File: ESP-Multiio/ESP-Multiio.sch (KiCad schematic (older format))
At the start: 40 parts, among them J1 Conn_01x10, SW1 SW_SPDT_MSM, SW2 SW_SPDT_MSM, SW3 SW_SPDT_MSM, SW4 SW_SPDT_MSM, U1 WeMos_D1_mini, U2 MCP23017_SP

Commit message: +IR
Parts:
- added C2: 100 nF, Capacitor_SMD:C_1206_3216Metric_Pad1.42x1.75mm_HandSolder, symbol Device:C
- added D-IR1: LED, LED_THT:LED_D3.0mm, symbol Device:LED
- added Q1: BC337, Package_TO_SOT_THT:TO-92_Inline, symbol Transistor_BJT:BC337
- added R10: 53 Ω, Resistor_SMD:R_1206_3216Metric_Pad1.42x1.75mm_HandSolder, symbol Device:R
- added R11: 33 kΩ, Resistor_SMD:R_1206_3216Metric_Pad1.42x1.75mm_HandSolder, symbol Device:R
- added R12: 100Ω, Resistor_SMD:R_1206_3216Metric_Pad1.42x1.75mm_HandSolder, symbol Device:R
- added R9: 2.1kΩ, Resistor_SMD:R_1206_3216Metric_Pad1.42x1.75mm_HandSolder, symbol Device:R
- added U4: TSOP1838, TSOP1838:TSOP18XX, symbol TSOP1838:TSOP1838
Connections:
- net +3V3: now also D-IR1.2 (A), R12.1
- net D0: now also R11.2, U4.OUT
- net D7: now also R9.2
- net GND: now also C2.2, Q1.3 (E), U4.GND
- net GPB0: now reaches SW1.3, U2.1 (GPB0)
- net GPB1: now reaches SW1.1, U2.2 (GPB1)
- net GPA0: now reaches R1.2, U2.21 (GPA0)
- net GPA1: now reaches R2.2, U2.22 (GPA1)
- net GPA2: now reaches R3.2, U2.23 (GPA2)
- net GPA3: now reaches R4.2, U2.24 (GPA3)
- net GPA4: now reaches R5.2, U2.25 (GPA4)
- net GPA5: now reaches R6.2, U2.26 (GPA5)
- net GPA6: now reaches R7.2, U2.27 (GPA6)
- net GPA7: now reaches R8.2, U2.28 (GPA7)
- net GPB2: now reaches SW2.3, U2.3 (GPB2)
- net GPB3: now reaches SW2.1, U2.4 (GPB3)
- net GPB4: now reaches SW3.3, U2.5 (GPB4)
- net GPB5: now reaches SW3.1, U2.6 (GPB5)
- net GPB6: now reaches SW4.3, U2.7 (GPB6)
- net GPB7: now reaches SW4.1, U2.8 (GPB7)
- new net: C2.1, R11.1, R12.2, U4.VCC (V+)
- new net: Q1.1 (C), R10.2
- new net: Q1.2 (B), R9.1
- new net: D-IR1.1 (K), R10.1
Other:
- moved on the sheet: D1, D2, D3, D4, D5, D6, D7, D8, R1, R2, R3, R4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

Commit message: Better switch-footprint, add twitter avatar, add github link
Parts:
- SW1, SW2, SW3, SW4: footprint Switch:Switch -> Switch:MTS-103
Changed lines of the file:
@@
 F 0 "SW4" V 7300 1098 50  0000 L CNN
 F 1 "SW_SPDT_MSM" H 7300 716 50  0001 C CNN
-F 2 "Switch:Switch" H 7300 950 50  0001 C CNN
+F 2 "Switch:MTS-103" H 7300 950 50  0001 C CNN
 F 3 "~" H 7300 950 50  0001 C CNN
 	1    7300 950
@@
 F 0 "SW3" V 7000 1098 50  0000 L CNN
 F 1 "SW_SPDT_MSM" H 7000 716 50  0001 C CNN
-F 2 "Switch:Switch" H 7000 950 50  0001 C CNN
+F 2 "Switch:MTS-103" H 7000 950 50  0001 C CNN
 F 3 "~" H 7000 950 50  0001 C CNN
 	1    7000 950
@@
 F 0 "SW2" V 6700 1098 50  0000 L CNN
 F 1 "SW_SPDT_MSM" H 6700 1144 50  0001 C CNN
-F 2 "Switch:Switch" H 6700 950 50  0001 C CNN
+F 2 "Switch:MTS-103" H 6700 950 50  0001 C CNN
 F 3 "~" H 6700 950 50  0001 C CNN
 	1    6700 950
@@
 F 0 "SW1" V 6350 1098 50  0000 L CNN
 F 1 "SW_SPDT_MSM" V 6395 1098 50  0001 L CNN
-F 2 "Switch:Switch" H 6350 950 50  0001 C CNN
+F 2 "Switch:MTS-103" H 6350 950 50  0001 C CNN
 F 3 "~" H 6350 950 50  0001 C CNN
 	1    6350 950

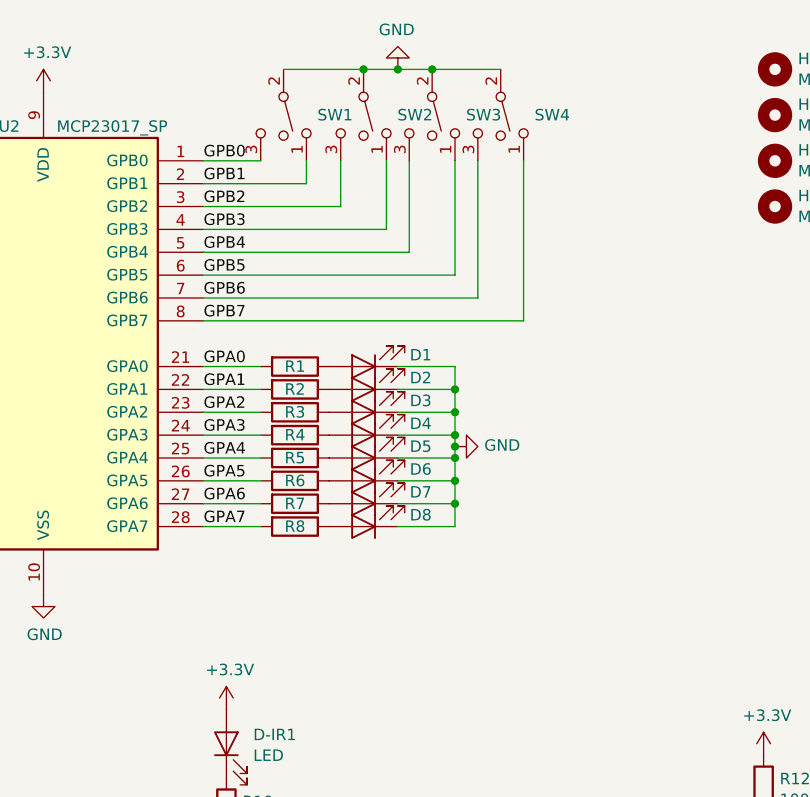
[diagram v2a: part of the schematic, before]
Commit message: Change board dimensions
Because the switches need to be further appart
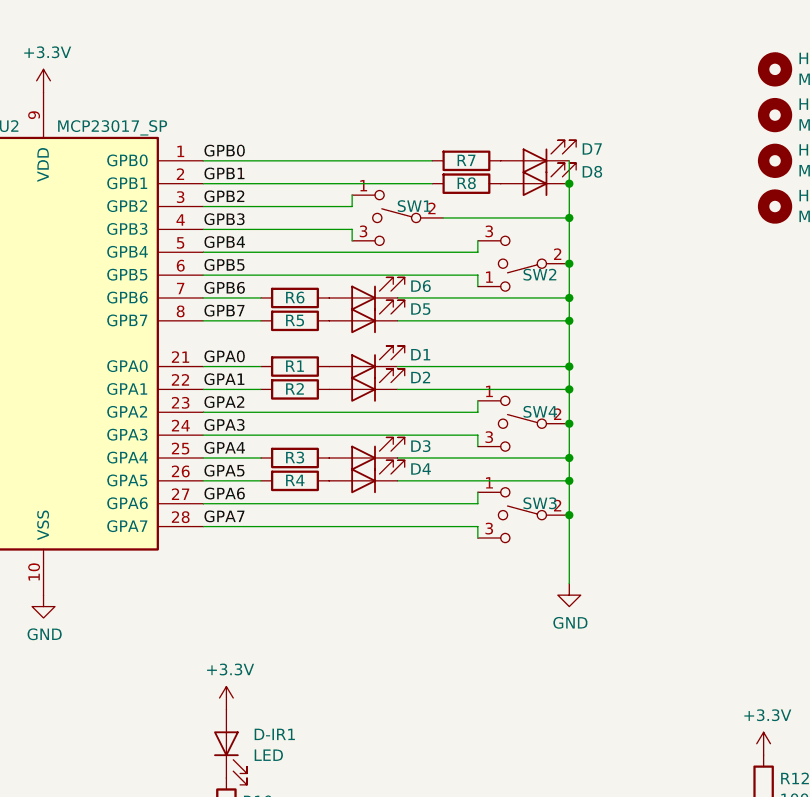
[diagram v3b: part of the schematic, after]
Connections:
- net GPA2: now also SW4.1; no longer R3.2
- net GPA3: now also SW4.3; no longer R4.2
- net GPA4: now also R3.2; no longer R5.2
- net GPA5: now also R4.2; no longer R6.2
- net GPA6: now also SW3.1; no longer R7.2
- net GPA7: now also SW3.3; no longer R8.2
- net GPB0: now also R7.2; no longer SW1.3
- net GPB1: now also R8.2; no longer SW1.1
- net GPB2: now also SW1.1; no longer SW2.3
- net GPB3: now also SW1.3; no longer SW2.1
- net GPB4: now also SW2.3; no longer SW3.3
- net GPB5: now also SW2.1; no longer SW3.1
- net GPB6: now also R6.2; no longer SW4.3
- net GPB7: now also R5.2; no longer SW4.1
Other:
- moved on the sheet: D3, D4, D5, D6, D7, D8, R3, R4, R5, R6, R7, R8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
